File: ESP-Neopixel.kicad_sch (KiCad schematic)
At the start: 72 parts, among them J1 CSP-USC16-TR, Q1 BC547, Q2 BC547, SW1 SW_Push, SW2 SW_Push, U1 CH340C, U2 AMS1117-3.3, U3 ESP32-WROOM-32E_(16MB)

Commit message: Changes some crap
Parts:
- added D26: 1N5819, Diode_SMD:D_SOD-323_HandSoldering, symbol Diode:1N5819
- added D27: Red, LED_SMD:LED_0805_2012Metric, symbol Device:LED
- added D28: Blue, LED_SMD:LED_0805_2012Metric, symbol Device:LED
- added R10, R9: 10k, Resistor_SMD:R_0805_2012Metric, symbol Device:R
- added R11: 1k, Resistor_SMD:R_0805_2012Metric, symbol Device:R
- added R12: 470, Resistor_SMD:R_0805_2012Metric, symbol Device:R
- C1, C11, C12, C13, C14, C15, C16, C17, C18, C19, C2, C20, C21, C22, C23, C24, C25, C3, C4, C5, C6, C7, C8, C9: footprint Capacitor_SMD:C_0805_2012Metric_Pad1.18x1.45mm_HandSolder -> Cap:Cap
- C10: footprint Capacitor_SMD:C_0805_2012Metric -> Cap:Cap
- C26, C27: value 100nF -> 0.1uf; footprint Capacitor_SMD:C_0805_2012Metric_Pad1.18x1.45mm_HandSolder -> Capacitor_SMD:C_0805_2012Metric
- C28: renamed from C29; value 100nf -> 0.1uf; footprint Capacitor_SMD:C_0805_2012Metric_Pad1.18x1.45mm_HandSolder -> Capacitor_SMD:C_0805_2012Metric
- C29: renamed from C28; value 100nf -> 0.1uf; footprint Capacitor_SMD:C_0805_2012Metric_Pad1.18x1.45mm_HandSolder -> Capacitor_SMD:C_0805_2012Metric
- C30, C31: renamed from C?; value 100nF -> 0.1uf; footprint Capacitor_SMD:C_0805_2012Metric_Pad1.18x1.45mm_HandSolder -> Capacitor_SMD:C_0805_2012Metric
- Q1, Q2: footprint Package_TO_SOT_THT:TO-92_Inline -> Package_TO_SOT_SMD:TSOT-23
- R1: renamed from R4; footprint Resistor_SMD:R_0805_2012Metric_Pad1.20x1.40mm_HandSolder -> Resistor_SMD:R_0805_2012Metric
- R2: renamed from R3; footprint Resistor_SMD:R_0805_2012Metric_Pad1.20x1.40mm_HandSolder -> Resistor_SMD:R_0805_2012Metric
- R3: renamed from R1; footprint Resistor_SMD:R_0805_2012Metric_Pad1.20x1.40mm_HandSolder -> Resistor_SMD:R_0805_2012Metric
- R4: renamed from R2; footprint Resistor_SMD:R_0805_2012Metric_Pad1.20x1.40mm_HandSolder -> Resistor_SMD:R_0805_2012Metric
- R5, R6, R7, R8: renamed from R?; footprint (none) -> Resistor_SMD:R_0805_2012Metric
- SW1: renamed from SW2; footprint Button_Switch_SMD:SW_DIP_SPSTx01_Slide_9.78x4.72mm_W8.61mm_P2.54mm -> Button_Switch_SMD:SW_SPST_B3U-1000P
- SW2: renamed from SW1; footprint Button_Switch_SMD:SW_DIP_SPSTx01_Slide_9.78x4.72mm_W8.61mm_P2.54mm -> Button_Switch_SMD:SW_SPST_B3U-1000P
- renumbered U2 to U1, J1 to U2, U1 to U3, U3 to U4
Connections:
- net +3.3V: now also R9.1
- net +5V: now also D26.2 (A), D27.2 (A); no longer C27.2, U1.3 (VI)
- net EN: now also R9.2
- net Earth: now also D28.1 (K), R10.1, R11.2
- net IO15: now also R10.2
- new net: C27.2, D26.1 (K), U1.3 (VI)
- new net: D28.2 (A), R12.2
- new net: D27.1 (K), R11.1
- new net IO2: R12.1
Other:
- moved on the sheet: C30, C31, R5, R6, U3

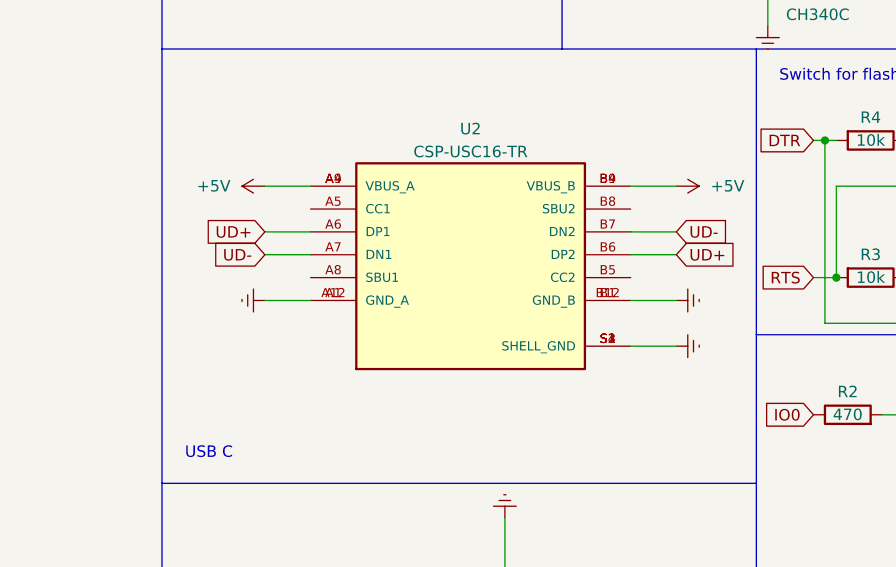
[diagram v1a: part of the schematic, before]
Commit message: Added 5.1k for PD
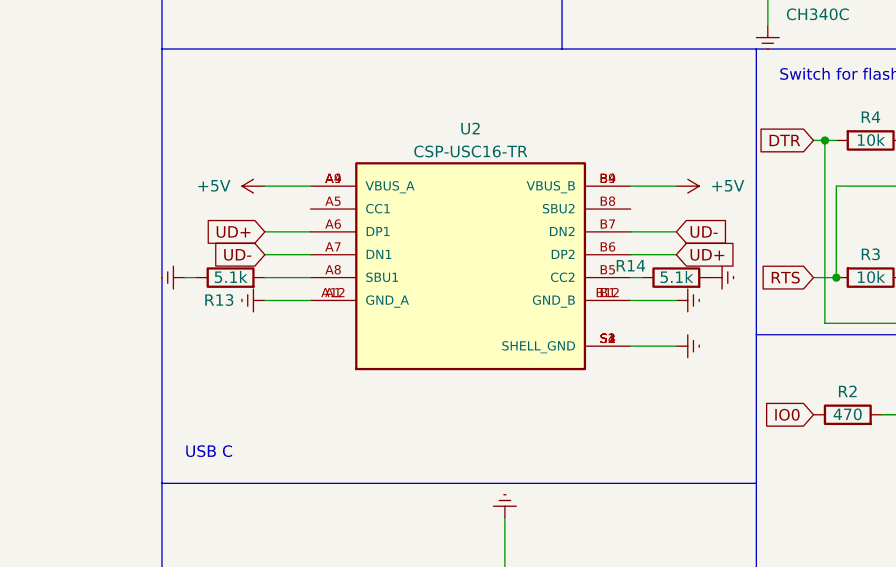
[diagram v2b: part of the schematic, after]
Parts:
- added R13, R14: 5.1k, symbol Device:R
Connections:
- net Earth: now also R13.1, R14.2
- net at U2.A8 (SBU1): now also R13.2
- net at U2.B5 (CC2): now also R14.1
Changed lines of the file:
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@@
     (stroke (width 0) (type default) (color 0 0 0 0))
   )
+  (wire (pts (xy 205.74 176.53) (xy 210.82 176.53))
+    (stroke (width 0) (type default) (color 0 0 0 0))
+  )
   (wire (pts (xy 264.16 35.56) (xy 269.24 35.56))
     (stroke (width 0) (type default) (color 0 0 0 0))
@@
     (stroke (width 0) (type default) (color 255 0 0 1))
   )
+  (wire (pts (xy 246.38 176.53) (xy 247.65 176.53))
+    (stroke (width 0) (type default) (color 0 0 0 0))
+  )
   (wire (pts (xy 218.44 66.04) (xy 223.52 66.04))
     (stroke (width 0) (type default) (color 0 0 0 0))
@@
     (stroke (width 0) (type default) (color 0 0 0 0))
   )
+  (wire (pts (xy 196.85 176.53) (xy 198.12 176.53))
+    (stroke (width 0) (type default) (color 0 0 0 0))
+  )
   (wire (pts (xy 24.13 124.46) (xy 24.13 125.73))
     (stroke (width 0) (type default) (color 255 0 0 1))
@@
     (pin "2")
   )
+  (symbol (lib_id "Device:R") (at 251.46 176.53 90) (unit 1)
+    (in_bom yes) (on_board yes)
+    (property "Reference" "R14" (id 0) (at 246.38 175.26 90))
+    (property "Value" "5.1k" (id 1) (at 251.46 176.53 90))
+    (property "Footprint" "" (id 2) (at 251.46 178.308 90)
+      (effects (font (size 1.27 1.27)) hide)
+    )
+    (property "Datasheet" "~" (id 3) (at 251.46 176.53 0)
+      (effects (font (size 1.27 1.27)) hide)
+    )
+    (pin "1")
+    (pin "2")
+  )
   (symbol (lib_id "power:Earth") (at 24.13 114.3 0) (unit 1)
     (in_bom yes) (on_board yes) (fields_autoplaced)
@@
     (pin "1")
   )
+  (symbol (lib_name "Earth_1") (lib_id "power:Earth") (at 196.85 176.53 270) (unit 1)
+    (in_bom yes) (on_board yes) (fields_autoplaced)
+    (property "Reference" "#PWR?" (id 0) (at 190.5 176.53 0)
+      (effects (font (size 1.27 1.27)) hide)
+    )
+    (property "Value" "Earth" (id 1) (at 193.04 176.53 0)
+      (effects (font (size 1.27 1.27)) hide)
+    )
+    (property "Footprint" "" (id 2) (at 196.85 176.53 0)
+      (effects (font (size 1.27 1.27)) hide)
+    )
+    (property "Datasheet" "~" (id 3) (at 196.85 176.53 0)
+      (effects (font (size 1.27 1.27)) hide)
+    )
+    (pin "1")
+  )
   (symbol (lib_id "Device:C") (at 275.59 137.16 90) (unit 1)
     (in_bom yes) (on_board yes)
@@
     (pin "2")
   )
+  (symbol (lib_name "Earth_2") (lib_id "power:Earth") (at 255.27 176.53 90) (unit 1)
+    (in_bom yes) (on_board yes) (fields_autoplaced)
+    (property "Reference" "#PWR?" (id 0) (at 261.62 176.53 0)
+      (effects (font (size 1.27 1.27)) hide)
+    )
+    (property "Value" "Earth" (id 1) (at 259.08 176.53 0)
+      (effects (font (size 1.27 1.27)) hide)
+    )
+    (property "Footprint" "" (id 2) (at 255.27 176.53 0)
+      (effects (font (size 1.27 1.27)) hide)
+    )
+    (property "Datasheet" "~" (id 3) (at 255.27 176.53 0)
+      (effects (font (size 1.27 1.27)) hide)
+    )
+    (pin "1")
+  )
   (symbol (lib_id "Device:C") (at 284.48 201.93 90) (unit 1)
     (in_bom yes) (on_board yes) (fields_autoplaced)
@@
     (pin "2")
   )
+  (symbol (lib_id "Device:R") (at 201.93 176.53 90) (unit 1)
+    (in_bom yes) (on_board yes)
+    (property "Reference" "R13" (id 0) (at 200.66 179.07 90))
+    (property "Value" "5.1k" (id 1) (at 201.93 176.53 90))
+    (property "Footprint" "" (id 2) (at 201.93 178.308 90)
+      (effects (font (size 1.27 1.27)) hide)
+    )
+    (property "Datasheet" "~" (id 3) (at 201.93 176.53 0)
+      (effects (font (size 1.27 1.27)) hide)
+    )
+    (pin "1")
+    (pin "2")
+  )
   (symbol (lib_id "Regulator_Linear:AMS1117-3.3") (at 232.41 223.52 180) (unit 1)
     (in_bom yes) (on_board yes) (fields_autoplaced)
@@
       (reference "#PWR0172") (unit 1) (value "Earth") (footprint "")
     )
+    (path "/a39d30d4-c33b-4c5f-8c23-6f890145bf85"
+      (reference "#PWR?") (unit 1) (value "Earth") (footprint "")
+    )
+    (path "/ca51468e-e0c2-402f-8bac-92972c8d5b7e"
+      (reference "#PWR?") (unit 1) (value "Earth") (footprint "")
+    )
     (path "/c573bf54-1cca-400c-b55f-e952b41b2535"
       (reference "C1") (unit 1) (value "0.1uf") (footprint "Cap:Cap")
@@
       (reference "R12") (unit 1) (value "470") (footprint "Resistor_SMD:R_0805_2012Metric")
     )
+    (path "/d988dbe6-594f-40d2-aad7-87dde38ef988"
+      (reference "R13") (unit 1) (value "5.1k") (footprint "")
+    )
+    (path "/81e48512-69e9-4a77-a8b4-ea57dbc83a48"
+      (reference "R14") (unit 1) (value "5.1k") (footprint "")
+    )
     (path "/2cc904a5-3565-4610-b0a3-af42b84e2a37"

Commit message: Fixed some crap (not all of it)
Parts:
- removed C30: 0.1uf, Capacitor_SMD:C_0805_2012Metric, symbol Device:C
- added C32: 1uf, Capacitor_SMD:C_0805_2012Metric, symbol Device:C
- R1, R2: value 470 -> 10k
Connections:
- net +3.3V: now also U3.16 (VCC)
- net +5V: no longer U3.16 (VCC)
- net DTR: now also U3.13 (~{DTR})
- net EN: now also C32.2
- net Earth: now also C32.1; no longer C26.1, C27.1, U1.1 (GND)
- net RX: now also R6.2; no longer R5.2
- net TX: now also R5.2; no longer R6.2
- net at U2.A5 (CC1): now also R13.2
- net at U2.A8 (SBU1): no longer R13.2
- new net GNDREF: C26.1, C27.1, U1.1 (GND)
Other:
- moved on the sheet: C26, C27, D26, R13, R9, U1

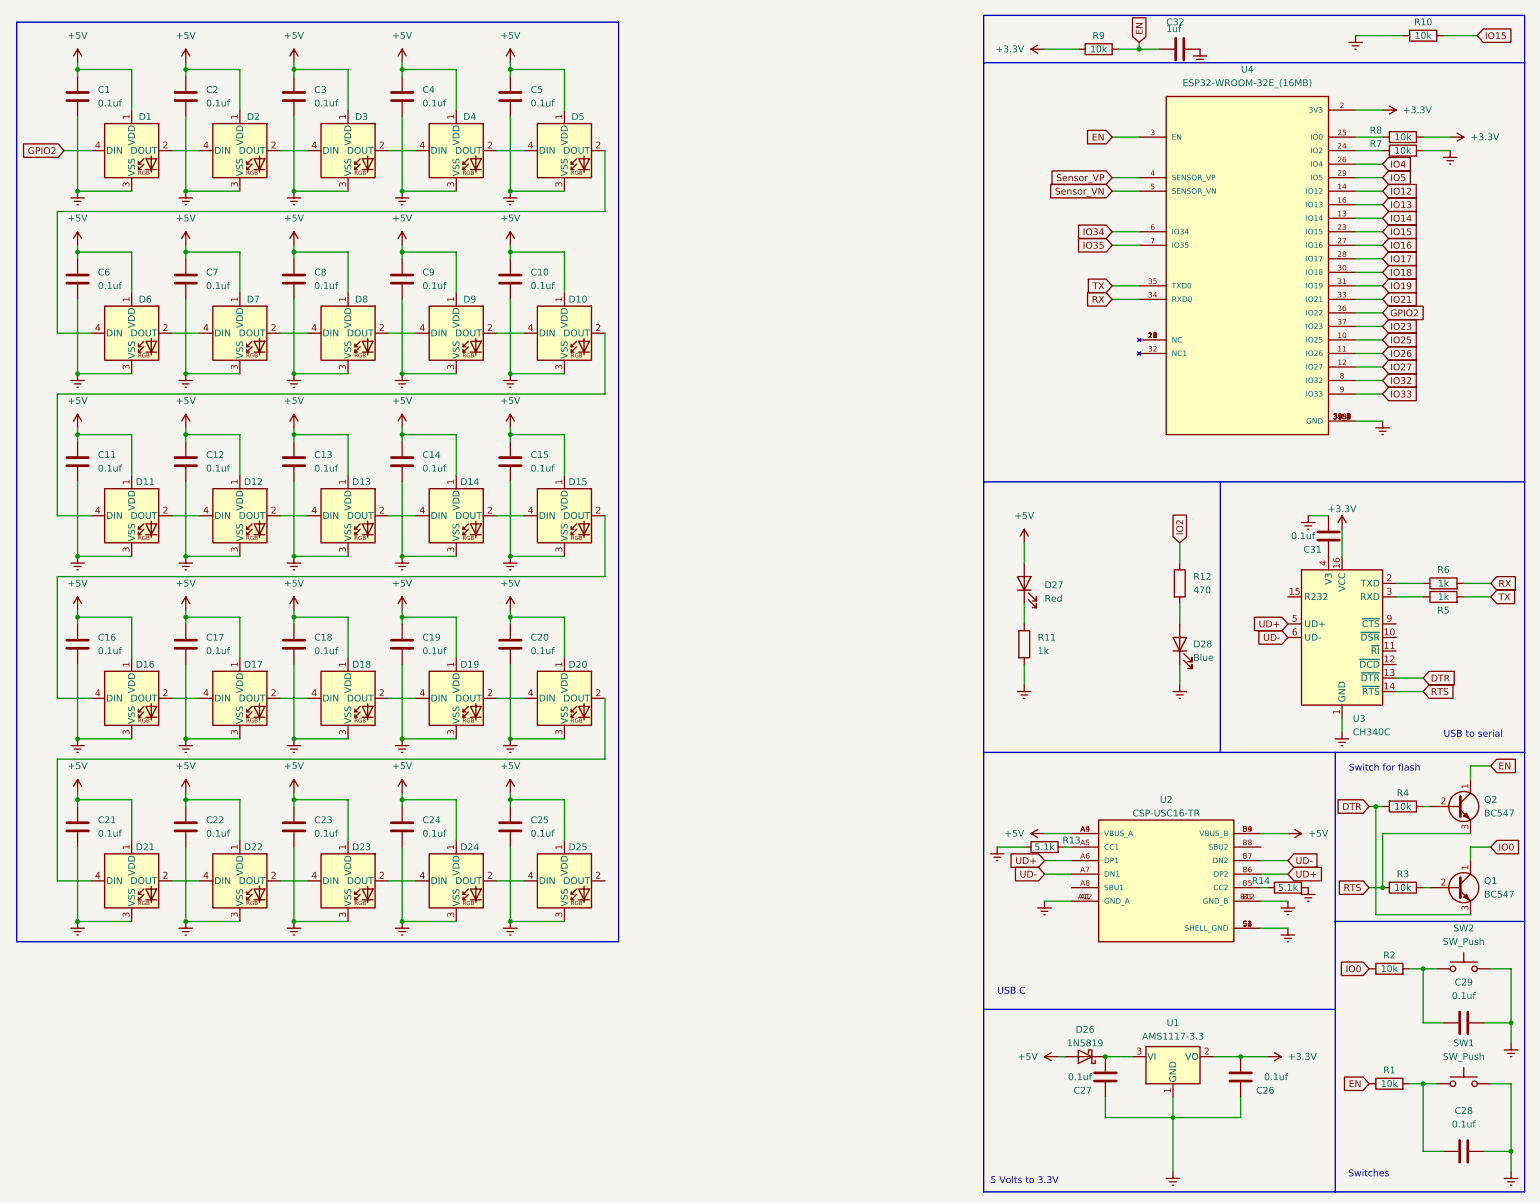
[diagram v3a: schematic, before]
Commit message: Added tvs diodes
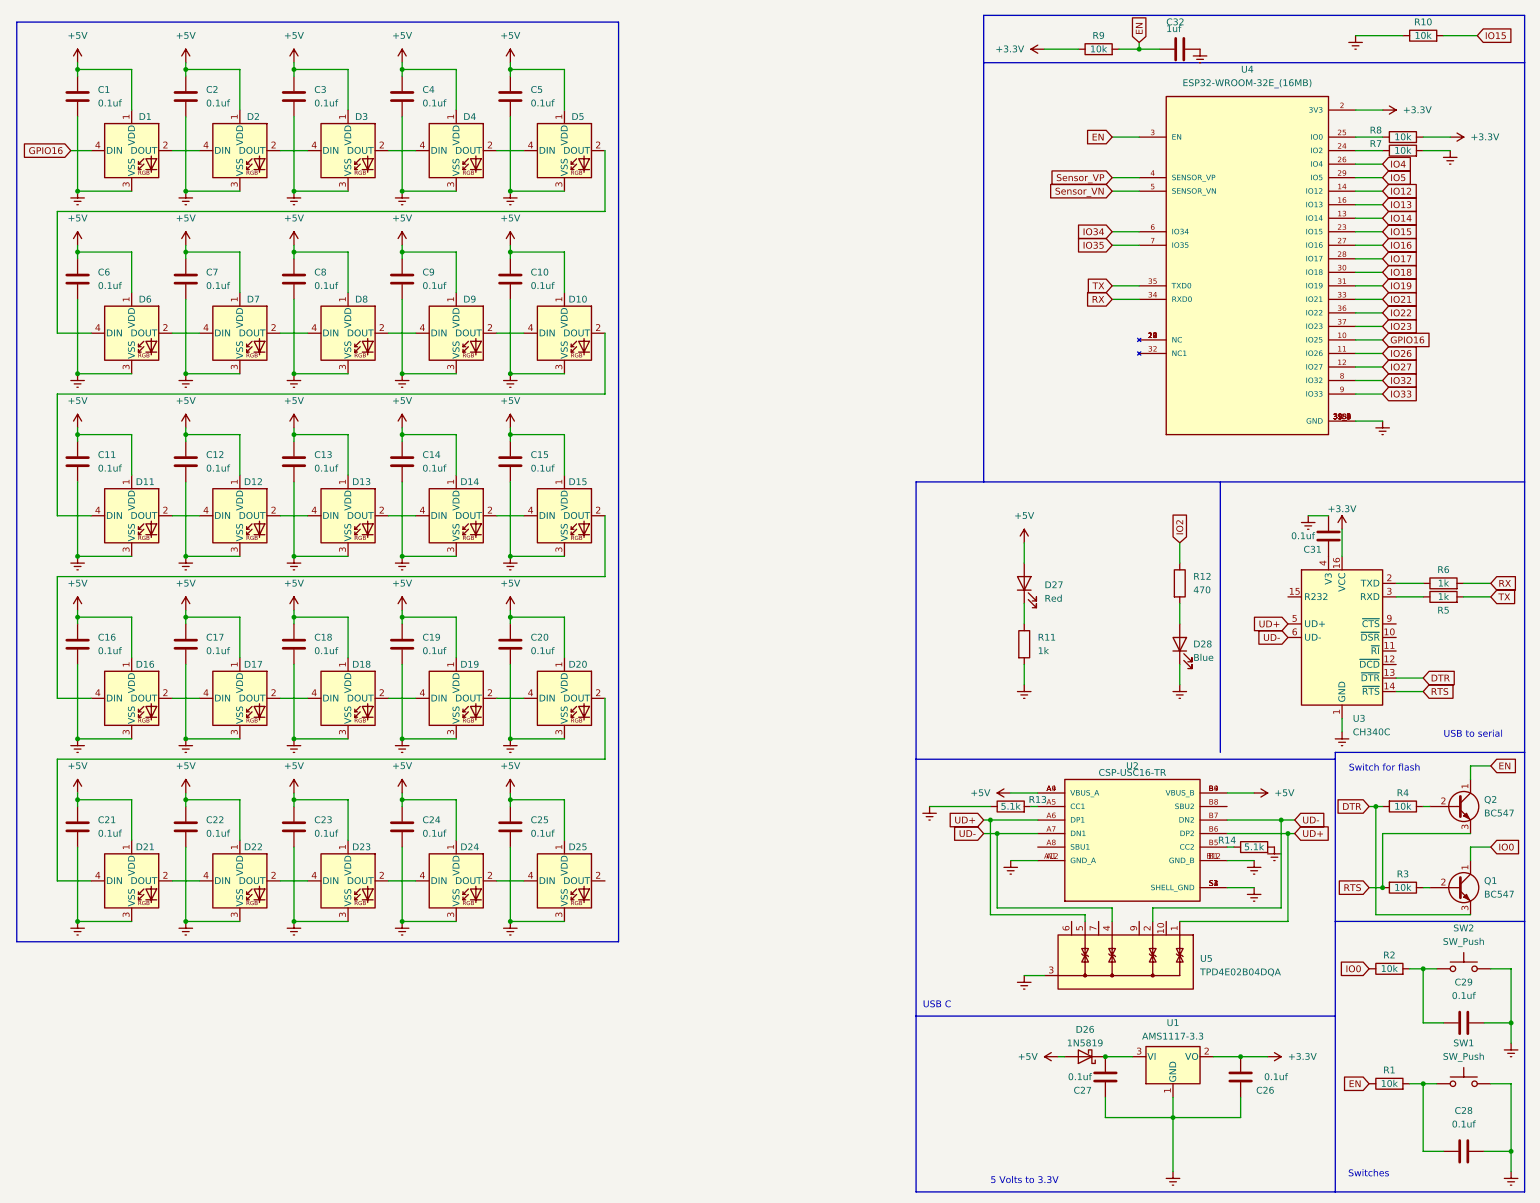
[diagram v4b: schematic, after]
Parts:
- added U5: TPD4E02B04DQA, Package_SON:USON-10_2.5x1.0mm_P0.5mm, symbol Power_Protection:TPD4E02B04DQA
- R13, R14: footprint (none) -> Resistor_SMD:R_0805_2012Metric
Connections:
- net IO25 is gone; now on net GPIO16: U4.10 (IO25)
- net Earth: now also U5.3 (G), U5.8 (G)
- net UD+: now also U5.1 (IO1), U5.5 (IO4)
- net UD-: now also U5.2 (IO2), U5.4 (IO3)
- net GPIO2 renamed GPIO16
- net GPIO16: no longer U4.36 (IO22)
- new net IO22: U4.36 (IO22)
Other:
- moved on the sheet: R13, R14, U2

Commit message: Changed AMS1117 to AZ1117IH
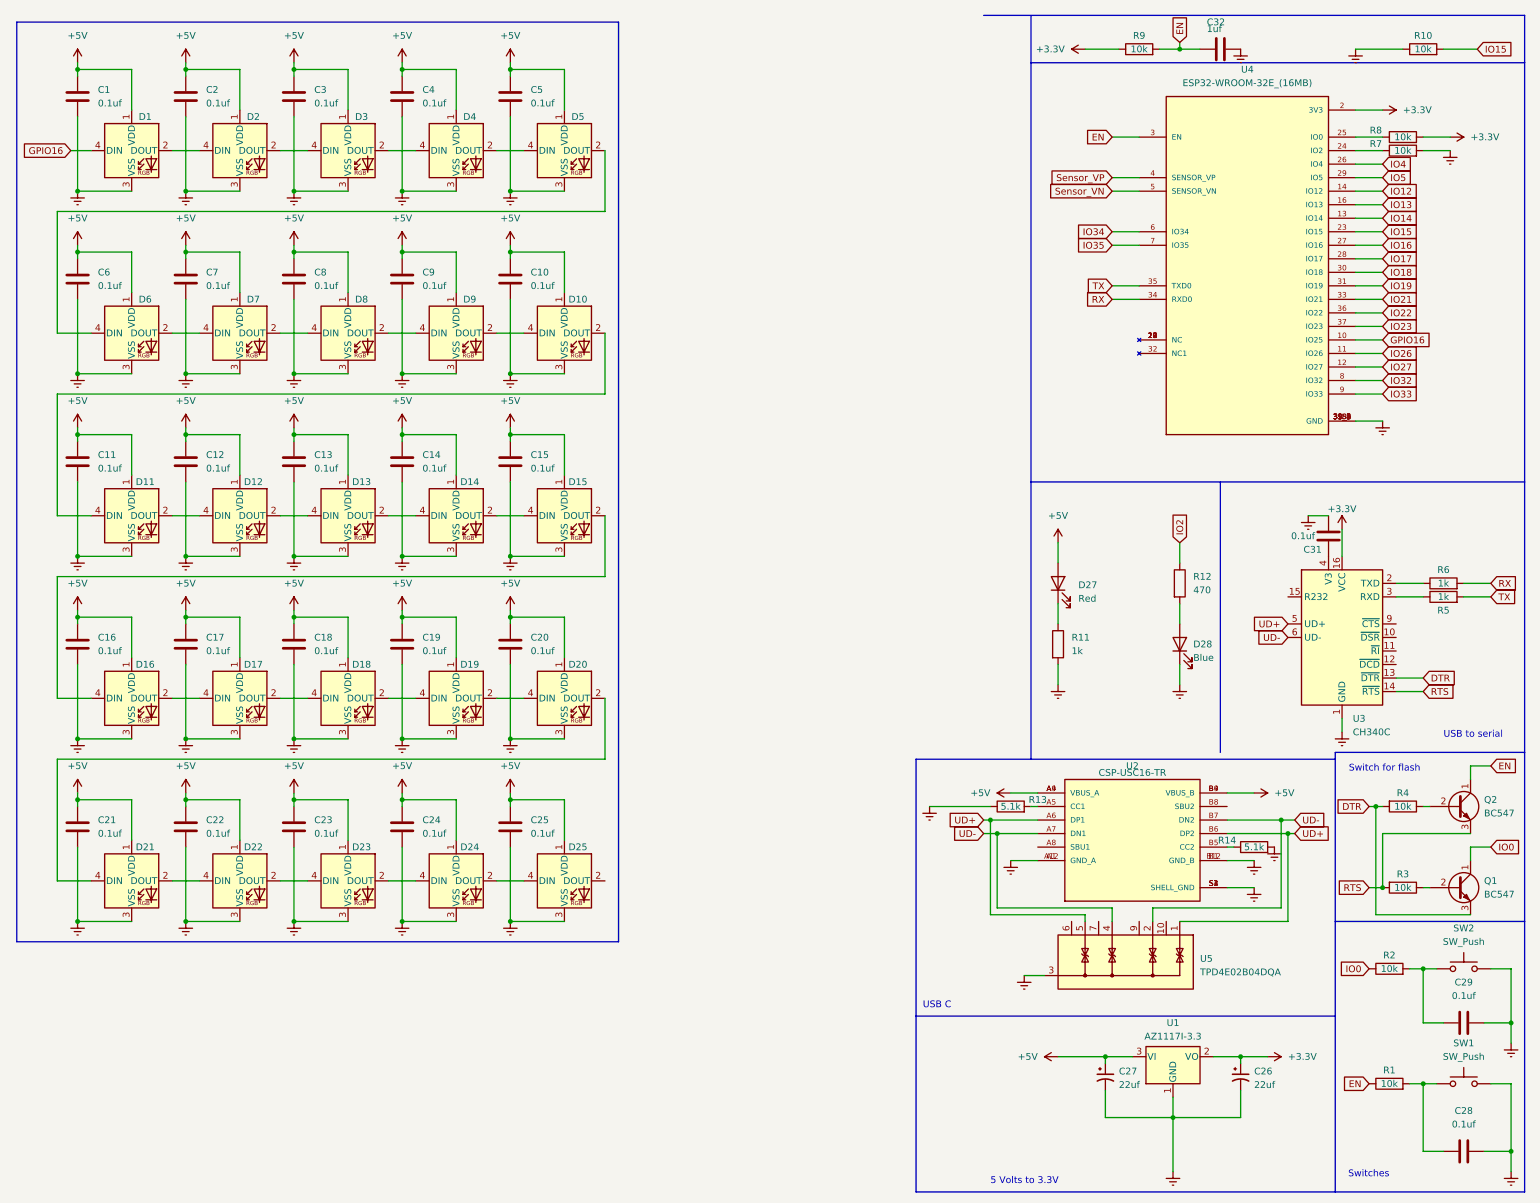
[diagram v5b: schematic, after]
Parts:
- removed C26, C27: 0.1uf, Capacitor_SMD:C_0805_2012Metric, symbol Device:C
- removed D26: 1N5819, Diode_SMD:D_SOD-323_HandSoldering, symbol Diode:1N5819
- added C26, C27: 22uf, symbol Device:C_Polarized_Small_US
- U1: value AMS1117-3.3 -> AZ1117I-3.3; footprint Package_TO_SOT_SMD:SOT-223-3_TabPin2 -> Package_TO_SOT_SMD:SOT-223
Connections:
- net +3.3V: now also C26.1
- net +5V: now also U1.3 (VI), C27.1
- net GNDREF: now also C26.2, C27.2
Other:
- moved on the sheet: C32, D27, R10, R11, R9
